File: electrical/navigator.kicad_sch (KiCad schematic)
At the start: 7 parts

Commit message: Upgraded G3X Touch to Axis
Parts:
- GAD29, GPS175, GPS175_CONFIG: value ~ -> (none)
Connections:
- net ADSB_SERIAL_GND: now also GPS175.P1751_10 (ETHERNET_TX_P)
- net ADSB_SERIAL_IN: now also GPS175.P1751_11 (ETHERNET_RX_P)
- net ETHERNET_OUT_B: now reaches GPS175.P1751_32 (ETHERNET_TX_N)
- net ETHERNET_IN_B: now reaches GPS175.P1751_33 (ETHERNET_RX_N)
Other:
- note added: "To G5 MapMX 57600 Page 24-38"
- note removed: "Only using MapMX to GDU 460, so that can get traffic & weather on the GPS 175. This means, won't be able to move flight plans to/from G3X. Can still BT to GPS 175 and do it from the iPad."
- note removed: "To GDU 460 MapMX 57600 Page 24-38"

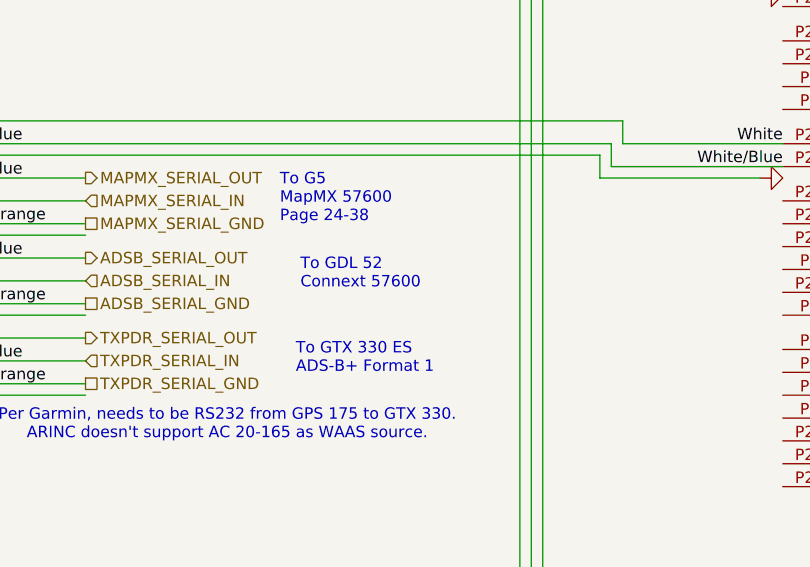
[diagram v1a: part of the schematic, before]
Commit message: Updated wiring to just do GDU Bat Lead leader. Also, keep pin 31 as effectively backup power like it was on G3X Touch
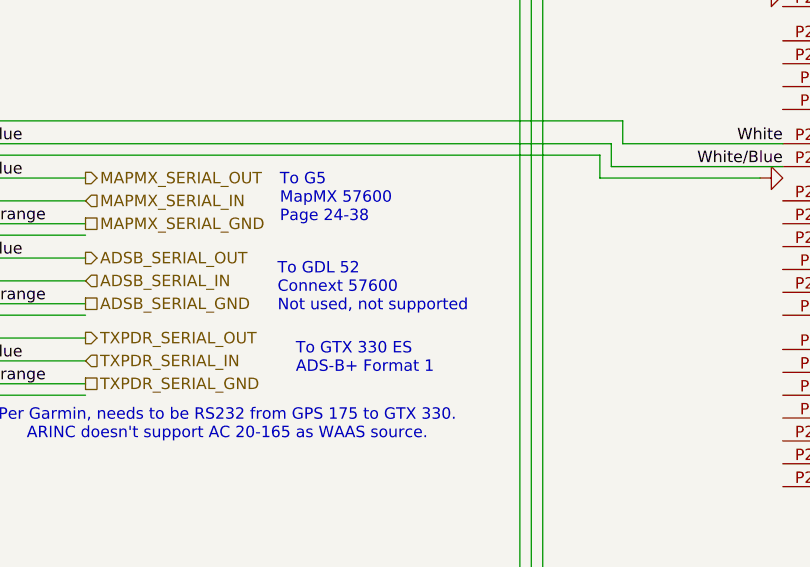
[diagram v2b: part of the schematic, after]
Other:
- note added: "To GDL 52 Connext 57600 Not used, not supported"
- note removed: "To GDL 52 Connext 57600"
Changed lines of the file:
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@@
 	(paper "A" portrait)
 	(title_block
-		(date "2026-08-01")
-		(rev "2.0")
+		(date "2026-08-18")
+		(rev "2.0.2")
 		(company "N877RV")
 	)
@@
 		)
 	)
-	(text "To GDL 52\nConnext 57600"
+	(text "To GDL 52\nConnext 57600\nNot used, not supported"
 		(exclude_from_sim no)
-		(at 105.156 87.376 0)
+		(at 102.616 89.916 0)
 		(effects
 			(font
